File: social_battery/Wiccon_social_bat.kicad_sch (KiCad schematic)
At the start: 20 parts, among them J1 SAO, SW1 Change, U1 CH32V003

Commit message: Change LCSC number of 100n capacitor on social battery
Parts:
- C1, C2: LCSC C466613 -> C307331
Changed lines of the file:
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@@
 			)
 		)
-		(property "LCSC" "C466613"
+		(property "LCSC" "C307331"
 			(at 104.14 38.1 0)
 			(effects
@@
 			)
 		)
-		(property "LCSC" "C466613"
+		(property "LCSC" "C307331"
 			(at 92.71 38.1 0)
 			(effects

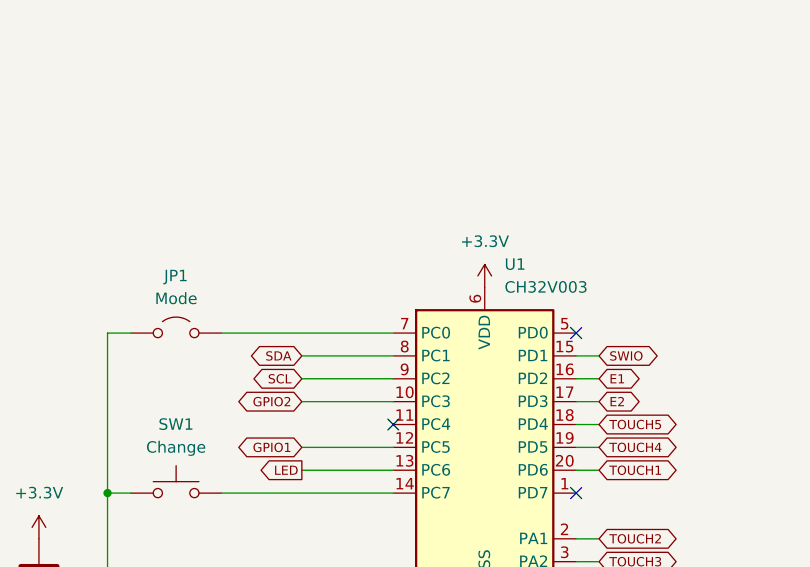
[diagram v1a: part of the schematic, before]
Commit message: Add 100k pull-up to SDA on social battery and use correct footprint for battery holder on SAO nametag
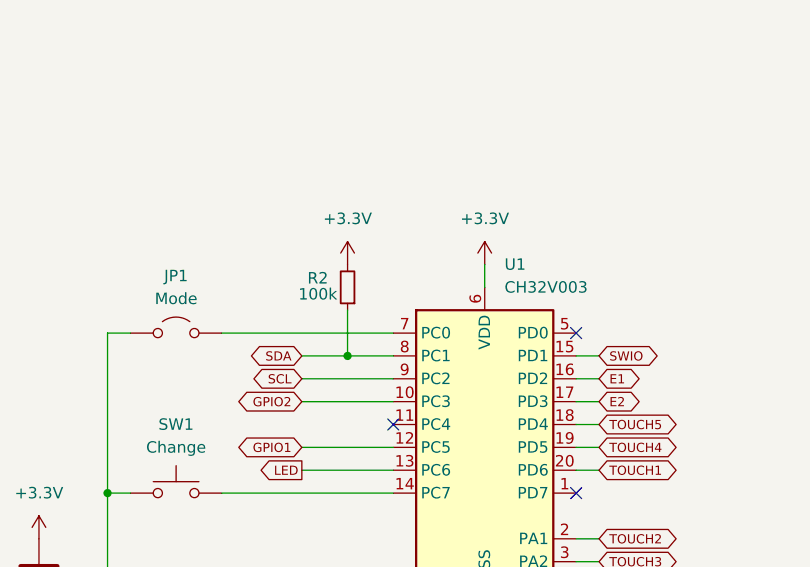
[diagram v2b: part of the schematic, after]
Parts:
- added R2: 100k, Resistor_SMD:R_0402_1005Metric, symbol Device:R_Small
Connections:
- net +3.3V: now also R2.2
- net SDA: now also R2.1
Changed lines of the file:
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@@
 	(paper "A4")
 	(junction
+		(at 133.35 96.52)
+		(diameter 0)
+		(color 0 0 0 0)
+	)
+	(junction
 		(at 106.68 111.76)
 		(diameter 0)
@@
 	(wire
 		(pts
+			(xy 133.35 96.52) (xy 138.43 96.52)
+		)
+		(stroke
+			(width 0)
+			(type default)
+		)
+	)
+	(wire
+		(pts
 			(xy 161.29 109.22) (xy 158.75 109.22)
 		)
@@
 	(wire
 		(pts
-			(xy 128.27 96.52) (xy 138.43 96.52)
+			(xy 128.27 96.52) (xy 133.35 96.52)
+		)
+		(stroke
+			(width 0)
+			(type default)
+		)
+	)
+	(wire
+		(pts
+			(xy 148.59 86.36) (xy 148.59 88.9)
 		)
 		(stroke
@@
 	(wire
 		(pts
+			(xy 133.35 91.44) (xy 133.35 96.52)
+		)
+		(stroke
+			(width 0)
+			(type default)
+		)
+	)
+	(wire
+		(pts
 			(xy 119.38 93.98) (xy 138.43 93.98)
 		)
@@
 	(symbol
 		(lib_id "power:+3.3V")
+		(at 133.35 86.36 0)
+		(unit 1)
+		(exclude_from_sim no)
+		(in_bom yes)
+		(on_board yes)
+		(dnp no)
+		(fields_autoplaced yes)
+		(property "Reference" "#PWR024"
+			(at 133.35 90.17 0)
+			(effects
+				(font
+					(size 1.27 1.27)
+				)
+				(hide yes)
+			)
+		)
+		(property "Value" "+3.3V"
+			(at 133.35 81.28 0)
+			(effects
+				(font
+					(size 1.27 1.27)
+				)
+			)
+		)
+		(property "Footprint" ""
+			(at 133.35 86.36 0)
+			(effects
+				(font
+					(size 1.27 1.27)
+				)
+				(hide yes)
+			)
+		)
+		(property "Datasheet" ""
+			(at 133.35 86.36 0)
+			(effects
+				(font
+					(size 1.27 1.27)
+				)
+				(hide yes)
+			)
+		)
+		(property "Description" "Power symbol creates a global label with name \"+3.3V\""
+			(at 133.35 86.36 0)
+			(effects
+				(font
+					(size 1.27 1.27)
+				)
+				(hide yes)
+			)
+		)
+		(pin "1"
+		)
+		(instances
+			(project "Wiccon_social_bat"
+				(path "/575bcede-8866-4ca7-a1ba-9804eb5c9e06"
+					(reference "#PWR024")
+					(unit 1)
+				)
+			)
+		)
+	)
+	(symbol
+		(lib_id "power:+3.3V")
 		(at 45.72 76.2 90)
 		(unit 1)
@@
 	(symbol
 		(lib_id "power:+3.3V")
-		(at 148.59 88.9 0)
+		(at 148.59 86.36 0)
 		(unit 1)
 		(exclude_from_sim no)
@@
 		(fields_autoplaced yes)
 		(property "Reference" "#PWR019"
-			(at 148.59 92.71 0)
+			(at 148.59 90.17 0)
 			(effects
 				(font
@@
 		)
 		(property "Value" "+3.3V"
-			(at 148.59 83.82 0)
+			(at 148.59 81.28 0)
 			(effects
 				(font
@@
 		)
 		(property "Footprint" ""
-			(at 148.59 88.9 0)
+			(at 148.59 86.36 0)
 			(effects
 				(font
@@
 		)
 		(property "Datasheet" ""
-			(at 148.59 88.9 0)
+			(at 148.59 86.36 0)
 			(effects
 				(font
@@
 		)
 		(property "Description" "Power symbol creates a global label with name \"+3.3V\""
-			(at 148.59 88.9 0)
+			(at 148.59 86.36 0)
 			(effects
 				(font
@@
 					(unit 1)
 				)
+			)
+		)
+	)
+	(symbol
+		(lib_id "Device:R_Small")
+		(at 133.35 88.9 180)
+		(unit 1)
+		(exclude_from_sim no)
+		(in_bom yes)
+		(on_board yes)
+		(dnp no)
+		(property "Reference" "R2"
+			(at 130.048 87.884 0)
+			(effects
+				(font
+					(size 1.27 1.27)
+				)
+			)
+		)
+		(property "Value" "100k"
+			(at 130.048 89.662 0)
+			(effects
+				(font
+					(size 1.27 1.27)
+				)
+			)
+		)
+		(property "Footprint" "Resistor_SMD:R_0402_1005Metric"
+			(at 133.35 88.9 0)
+			(effects
+				(font
+					(size 1.27 1.27)
+				)
+				(hide yes)
+			)
+		)
+		(property "Datasheet" ""
+			(at 133.35 88.9 0)
+			(effects
+				(font
+					(size 1.27 1.27)
+				)
+				(hide yes)
+			)
+		)
+		(property "Description" ""
+			(at 133.35 88.9 0)
+			(effects
+				(font
+					(size 1.27 1.27)
+				)
+				(hide yes)
+			)
+		)
+		(property "LCSC" "C25741"
+			(at 133.35 88.9 0)
+			(effects
+				(font
+					(size 1.27 1.27)
+				)
+				(hide yes)
+			)
+		)
+		(pin "2"
+		)
+		(pin "1"
+		)
+		(instances
+			(project "Wiccon_social_bat"
+				(path "/575bcede-8866-4ca7-a1ba-9804eb5c9e06"
+					(reference "R2")
+					(unit 1)
+				)
